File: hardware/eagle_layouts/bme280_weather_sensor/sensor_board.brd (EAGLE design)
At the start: 13.4 x 10.4 mm, 10 parts, among them CN1 1X4-CLEANBIG, IC1 REG1117, T1 ZXMD63N03XSOT-363, U1 BME280

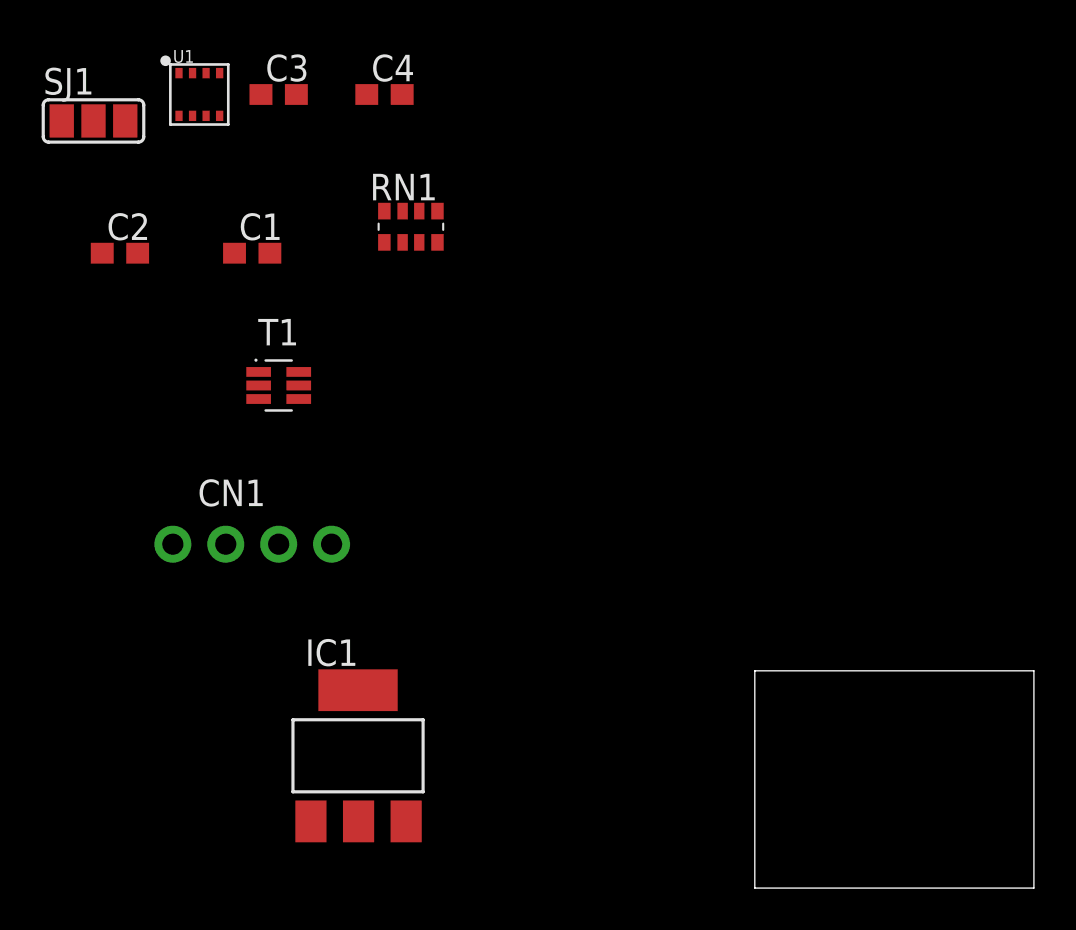
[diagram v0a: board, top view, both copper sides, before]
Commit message: Starting board layout for BME280 breakout
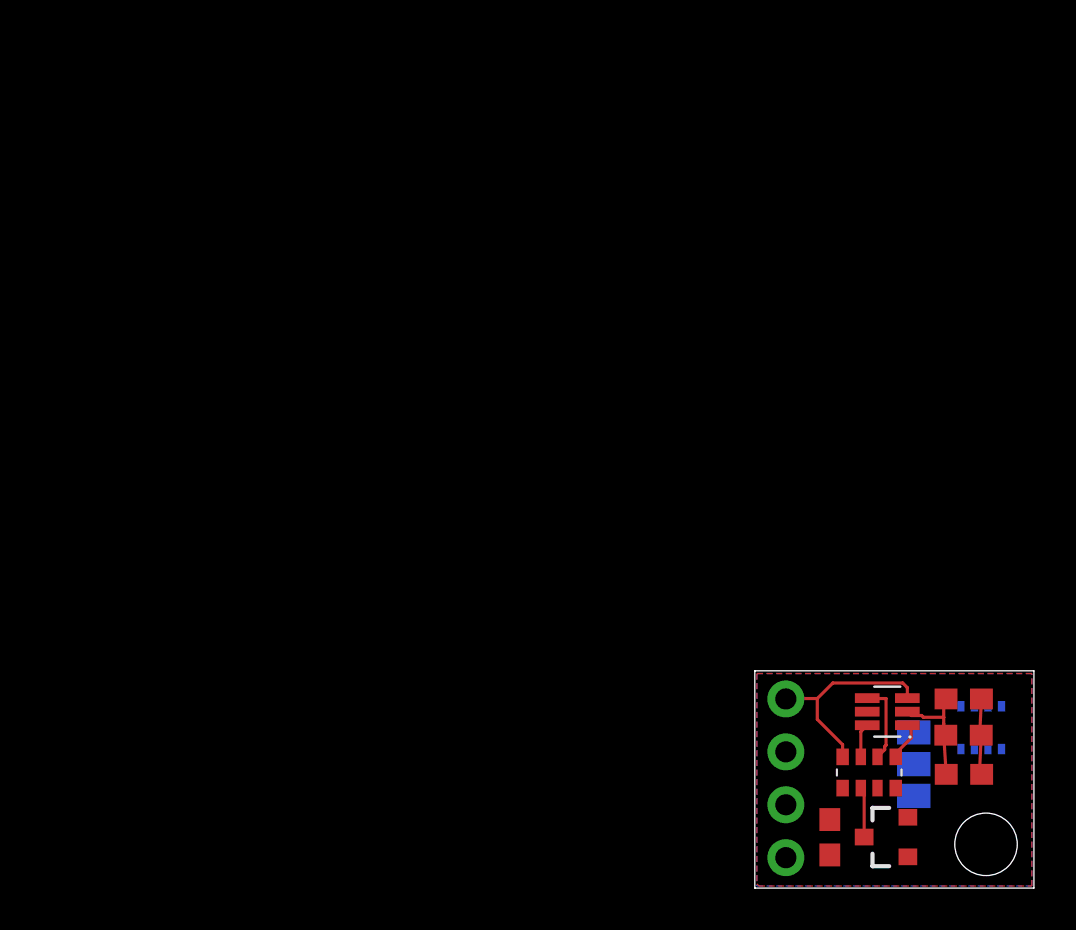
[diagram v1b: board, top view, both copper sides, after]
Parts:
- IC1: value REG1117 -> REG1117SOT-23-3; device burr-brown:SOT223 -> sensor_board:SOT23-3
- T1: device zetex:SOT-363 -> sensor_board:SOT-363
- moved SJ1 50.0 mm to (7.63, 5.95), flipped to the bottom, turned to 90 degrees
- moved U1 48.3 mm to (10.9, 7.70), flipped to the bottom, turned to 180 degrees
- moved C2 46.6 mm to (10.0, 7.34)
- moved C3 44.4 mm to (3.60, 2.44), turned to 90 degrees
- moved C4 42.9 mm to (10.0, 5.46)
- moved C1 40.3 mm to (10.0, 9.08)
- moved RN1 34.2 mm to (5.49, 5.55)
- moved T1 33.2 mm to (6.36, 8.47), turned to 180 degrees
- moved CN1 28.0 mm to (1.49, 5.27), turned to 90 degrees
- moved IC1 25.7 mm to (6.35, 2.45), turned to 90 degrees
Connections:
- removed net +3V3: C4.1, SJ1.3, U1.2, U1.6, U1.8
- net 3V3: now also C4.1, RN1.3, RN1.4, SJ1.3, U1.2, U1.6, U1.8; no longer RN1.5, RN1.7
- net ASCL: now also RN1.7, T1.6; no longer RN1.3, T1.1
- net ASDA: now also RN1.8, T1.3; no longer RN1.1, T1.4
- net BSCL: now also RN1.5, T1.1; no longer RN1.4, T1.3
- net BSDA: now also RN1.6, T1.4; no longer RN1.2, T1.6
- net VIN: now also RN1.1, RN1.2; no longer RN1.6, RN1.8
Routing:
- net ASDA: track 0.00 -> 10.0 mm
- net 3V3: track 0.00 -> 5.52 mm
- net GND: track 0.00 -> 4.80 mm
- net BSDA: track 0.00 -> 3.88 mm
- net VIN: track 0.00 -> 2.42 mm
- net BSCL: track 0.00 -> 1.73 mm
- net ASCL: track 0.00 -> 1.65 mm
- added copper zone on layer 1, net GND
- added copper zone on layer 16, net GND
